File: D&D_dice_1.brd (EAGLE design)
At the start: 27.9 x 31.8 mm, 28 parts, among them SW1 SPST_SWITCH, SW2 SPST_SWITCH, SW3 SPST_SWITCH, SW4 SPST_SWITCH, SW5 SPST_SWITCH, SW6 SPST_SWITCH, U1 ATMEGA168

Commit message: Board, code improvement.
Optimized the code, and improved the board a bit.
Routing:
- net GND: track 50.9 -> 71.2 mm
- net V+: track 91.2 -> 92.3 mm
- net RANDOM_OUT: track 30.1 -> 31.2 mm
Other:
- board text added: "Dice Roller"
- board text removed: "D&D Roller"

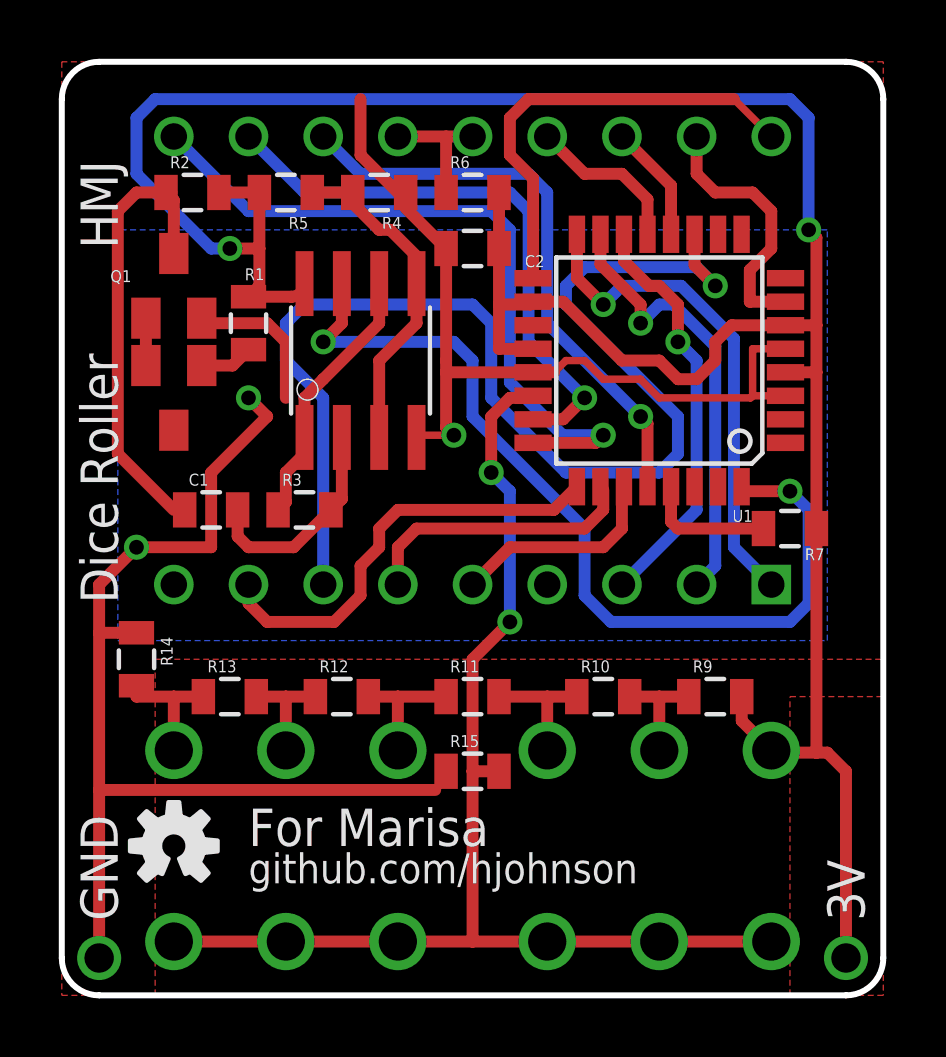
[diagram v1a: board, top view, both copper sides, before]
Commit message: Major commit: TESTED
Boards re-jiggered with bigger 0805 pads, because the small ones were
nightmarish. Code also much improved: It now actually works!
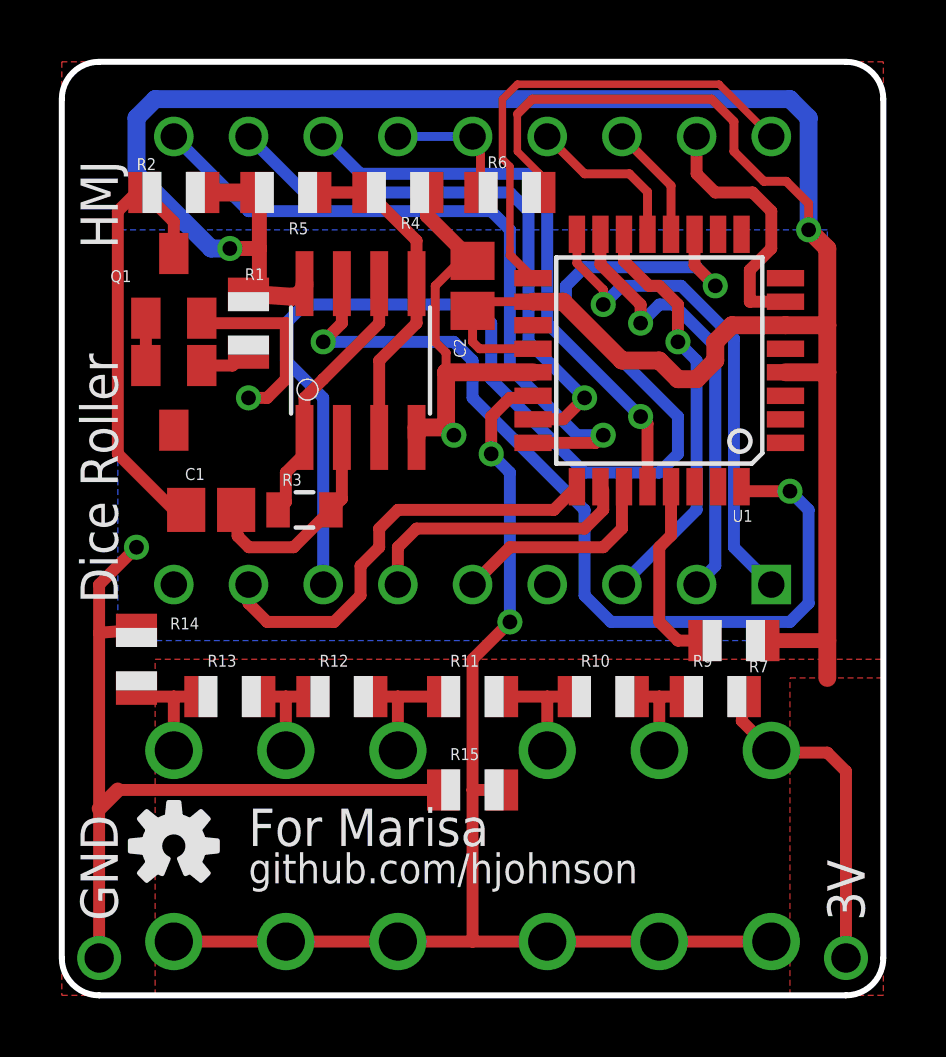
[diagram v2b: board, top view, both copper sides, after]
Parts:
- C1, C2: device SparkFun:0805 -> adafruit:C0805
- R1, R10, R11, R12, R13, R14, R15, R2, R4, R5, R6, R7, R9: device SparkFun:0805 -> adafruit:R0805
- moved R7 4.26 mm to (22.9, 12.1)
- moved C2 1.27 mm to (14.0, 24.1), turned to 270 degrees
- moved R6 1.27 mm to (15.2, 27.3)
- moved R2 0.64 mm to (3.81, 27.3)
- moved R15 0.63 mm to (14.0, 6.99)
- moved R4 0.63 mm to (11.4, 27.3)
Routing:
- net GND: track 71.2 -> 48.9 mm
- net V+: track 92.3 -> 106.9 mm
- net /RES: track 4.43 -> 6.57 mm
- net SCK: track 15.5 -> 16.6 mm
- net N$11: track 5.35 -> 4.56 mm
- net N$2: track 15.7 -> 15.0 mm

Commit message: Slight tweaks to the board to make it easier to solder.
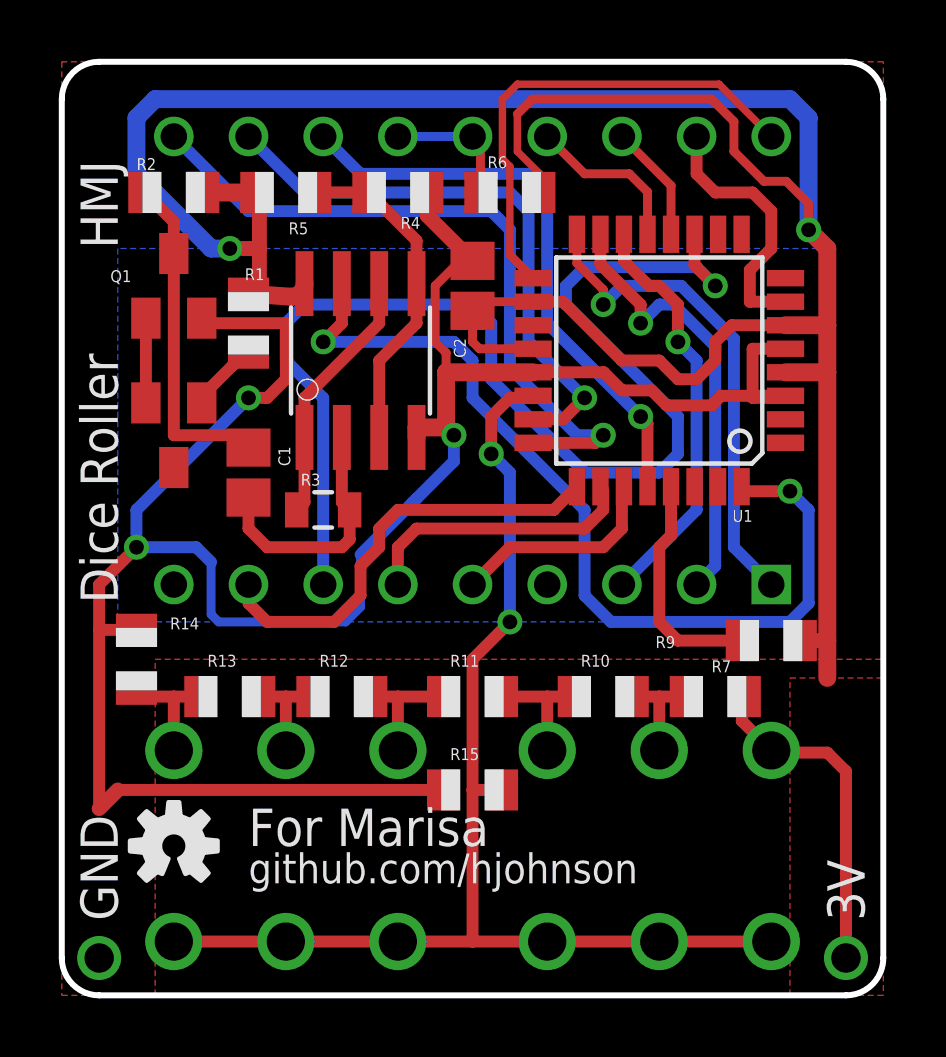
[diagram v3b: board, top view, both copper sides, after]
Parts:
- moved C1 1.80 mm to (6.35, 17.8), turned to 270 degrees
- moved R7 1.27 mm to (24.1, 12.1)
- moved U$1 1.27 mm to (3.81, 19.1)
- moved R3 0.63 mm to (8.89, 16.5)
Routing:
- net GND: track 48.9 -> 80.7 mm
- net N$2: track 15.0 -> 11.7 mm
- net V+: track 106.9 -> 105.7 mm
- net N$1: track 1.61 -> 2.88 mm
- net /RES: track 6.57 -> 7.84 mm
- net N$4: track 7.37 -> 8.45 mm
- net N$3: track 1.75 -> 2.40 mm

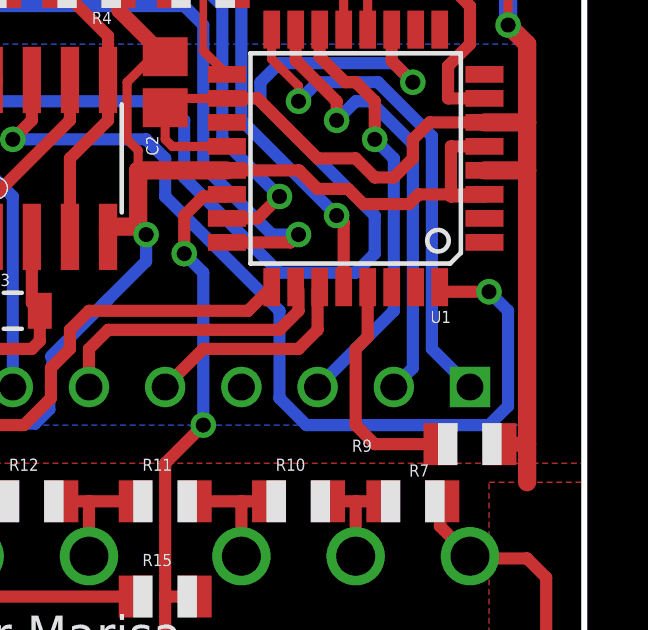
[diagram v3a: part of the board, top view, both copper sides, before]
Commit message: Added test pads for reset, lightly shifted around a few resistors.
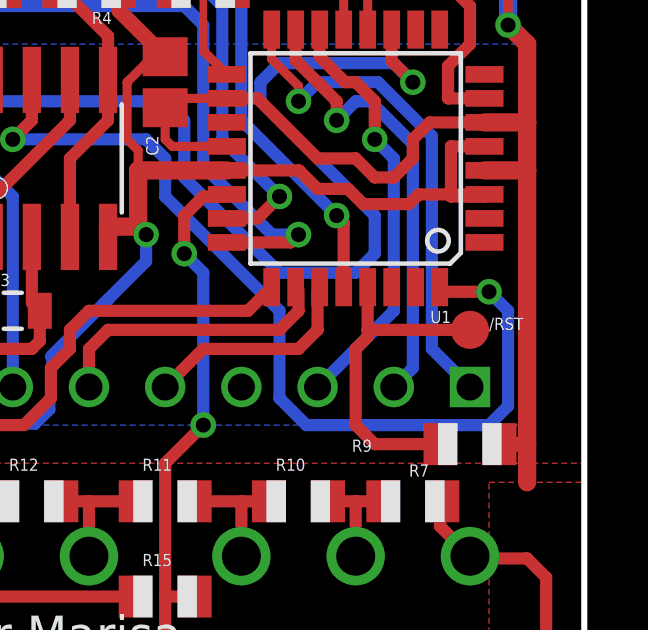
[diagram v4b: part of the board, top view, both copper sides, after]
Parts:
- added TP1: TPB1,27, testpad:B1,27
- IC1: value (none) -> MCP6282-E/SN-ND
- R15: value (none) -> 100K
- R6: value 470 -> 470R
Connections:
- net /RES: now also TP1.TP
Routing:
- net /RES: track 7.84 -> 11.2 mm
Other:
- board text added: "/RST"
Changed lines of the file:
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@@
 <wire x1="8.255" y1="22.86" x2="8.255" y2="20.955" width="0.254" layer="41"/>
 <wire x1="2.54" y1="6.35" x2="12.065" y2="6.35" width="0.254" layer="41"/>
+<text x="24.765" y="15.875" size="0.4064" layer="21">/RST</text>
 </plain>
 <attributes>
@@
 </autorouter>
 <elements>
-<element name="IC1" library="burr-brown" package="SO08" value="" x="10.16" y="21.59" smashed="yes">
+<element name="IC1" library="burr-brown" package="SO08" value="MCP6282-E/SN-ND" x="10.16" y="21.59" smashed="yes">
 <attribute name="OC_NEWARK" value="36K7581" x="38.1" y="-2.54" size="1.778" layer="27" display="off"/>
 <attribute name="MPN" value="OPA2340UA" x="38.1" y="-2.54" size="1.778" layer="27" display="off"/>
 <attribute name="MF" value="TEXAS INSTRUMENTS" x="38.1" y="-2.54" size="1.778" layer="27" display="off"/>
 <attribute name="OC_FARNELL" value="1101541" x="38.1" y="-2.54" size="1.778" layer="27" display="off"/>
-<attribute name="VALUE" x="14.1605" y="19.558" size="1.27" layer="27" ratio="10" rot="R90"/>
 </element>
 <element name="U$1" library="hjohnson_library" package="SOT23" value="" x="3.81" y="19.05" smashed="yes" rot="R180">
@@
 <element name="U1" library="SparkFun" package="TQFP32-08" value="ATMEGA168" x="20.32" y="21.59" rot="R180"/>
 <element name="U$2" library="hjohnson_library" package="HDSP-521E" value="2DIGIT_7SEGMENT" x="13.97" y="21.59" rot="MR0"/>
-<element name="R6" library="adafruit" package="R0805" value="470" x="15.24" y="27.305" smashed="yes">
+<element name="R6" library="adafruit" package="R0805" value="470R" x="15.24" y="27.305" smashed="yes">
 <attribute name="NAME" x="14.478" y="28.1305" size="0.4064" layer="25"/>
 <attribute name="VALUE" x="16.764" y="27.178" size="0.4064" layer="27"/>
@@
 </element>
 <element name="U$3" library="SparkFun" package="OSHW-LOGO-S" value="OSHW-LOGOS" x="3.81" y="5.08"/>
-<element name="R15" library="adafruit" package="R0805" value="" x="13.97" y="6.985" smashed="yes">
+<element name="R15" library="adafruit" package="R0805" value="100K" x="13.97" y="6.985" smashed="yes">
 <attribute name="NAME" x="13.208" y="8.001" size="0.4064" layer="25"/>
 <attribute name="VALUE" x="13.208" y="4.699" size="1.27" layer="27"/>
+</element>
+<element name="TP1" library="testpad" package="B1,27" value="TPB1,27" x="24.13" y="15.875" smashed="yes">
+<attribute name="TP_SIGNAL_NAME" value="" x="23.495" y="13.97" size="1" layer="37"/>
+<attribute name="VALUE" x="23.495" y="15.113" size="0.0254" layer="27"/>
 </element>
 </elements>
@@
 <wire x1="20.955" y1="12.065" x2="20.32" y2="12.7" width="0.4064" layer="1"/>
 <wire x1="20.32" y1="12.7" x2="20.32" y2="15.24" width="0.4064" layer="1"/>
-<wire x1="20.72" y1="17.2974" x2="20.72" y2="15.64" width="0.4064" layer="1"/>
+<wire x1="20.72" y1="17.2974" x2="20.72" y2="15.875" width="0.4064" layer="1"/>
 <wire x1="20.72" y1="15.64" x2="20.32" y2="15.24" width="0.4064" layer="1"/>
+<contactref element="TP1" pad="TP"/>
+<wire x1="24.13" y1="15.875" x2="20.72" y2="15.875" width="0.4064" layer="1"/>
+<wire x1="20.72" y1="15.875" x2="20.72" y2="15.64" width="0.4064" layer="1"/>
 </signal>
 <signal name="RX">

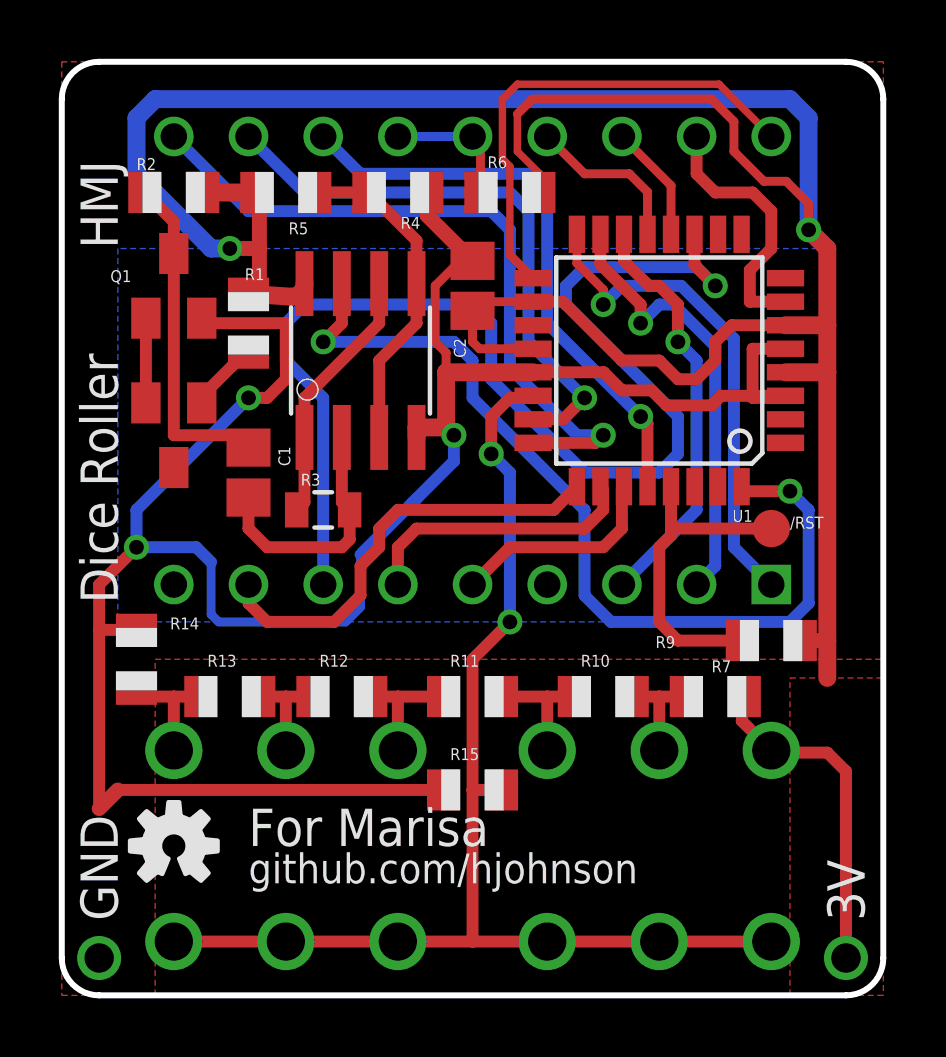
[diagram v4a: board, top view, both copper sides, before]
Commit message: Rotated a capacitor to make schematic look better, and added the schematic pdf.
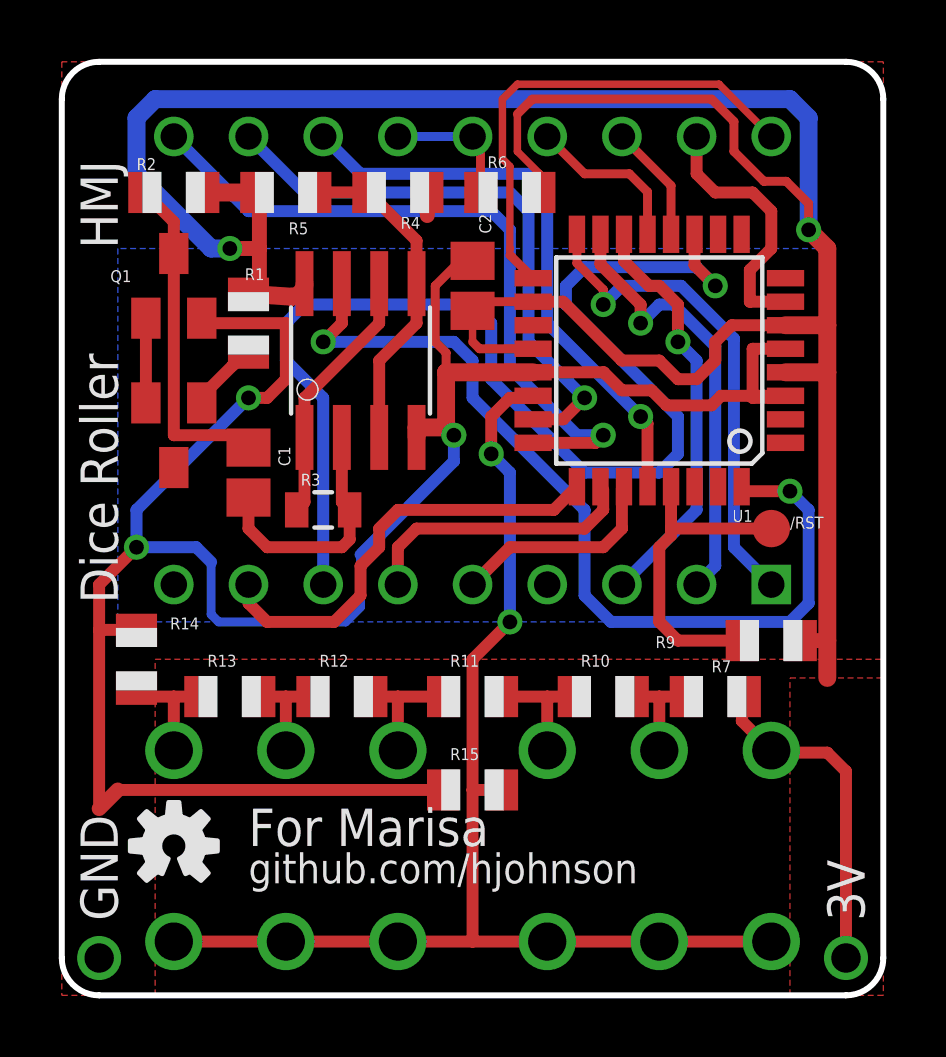
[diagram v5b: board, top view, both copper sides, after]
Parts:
- turned C2 to 90 degrees
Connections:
- net GND: now also C2.2; no longer C2.1
- net V+: now also C2.1; no longer C2.2
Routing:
- net GND: track 80.7 -> 78.1 mm
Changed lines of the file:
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@@
 <attribute name="VALUE" x="7.874" y="18.669" size="0.4064" layer="27" rot="R270"/>
 </element>
-<element name="C2" library="adafruit" package="C0805" value=".1uF" x="13.97" y="24.13" smashed="yes" rot="R270">
-<attribute name="NAME" x="13.335" y="22.352" size="0.4064" layer="25" rot="R270"/>
-<attribute name="VALUE" x="13.843" y="22.606" size="0.4064" layer="27" rot="R270"/>
+<element name="C2" library="adafruit" package="C0805" value=".1uF" x="13.97" y="24.13" smashed="yes" rot="R90">
+<attribute name="NAME" x="14.605" y="25.908" size="0.4064" layer="25" rot="R90"/>
+<attribute name="VALUE" x="14.097" y="25.654" size="0.4064" layer="27" rot="R90"/>
 </element>
 <element name="U1" library="SparkFun" package="TQFP32-08" value="ATMEGA168" x="20.32" y="21.59" rot="R180"/>
@@
 <contactref element="U1" pad="6"/>
 <contactref element="R6" pad="2"/>
-<contactref element="C2" pad="2"/>
 <contactref element="R7" pad="2"/>
 <wire x1="8.255" y1="24.2062" x2="8.255" y2="23.495" width="0.4064" layer="1"/>
@@
 <wire x1="16.0274" y1="21.99" x2="14.205" y2="21.99" width="0.3048" layer="1"/>
 <wire x1="14.205" y1="21.99" x2="13.97" y2="22.225" width="0.3048" layer="1"/>
-<wire x1="13.97" y1="22.225" x2="13.97" y2="23.28" width="0.3048" layer="1"/>
 <wire x1="16.0274" y1="23.59" x2="14.28" y2="23.59" width="0.3048" layer="1"/>
-<wire x1="14.28" y1="23.59" x2="13.97" y2="23.28" width="0.3048" layer="1"/>
 <wire x1="16.24" y1="27.305" x2="16.24" y2="27.448" width="0.3048" layer="1"/>
 <wire x1="15.494" y1="29.972" x2="16.002" y2="30.48" width="0.3048" layer="1"/>
@@
 <wire x1="6.72" y1="27.205" x2="6.62" y2="27.305" width="0.508" layer="1"/>
 <wire x1="5.715" y1="25.4" x2="6.72" y2="25.4" width="0.508" layer="1"/>
+<contactref element="C2" pad="1"/>
+<wire x1="13.97" y1="22.225" x2="13.97" y2="23.28" width="0.254" layer="1"/>
+<wire x1="14.28" y1="23.59" x2="13.97" y2="23.59" width="0.254" layer="1"/>
+<wire x1="13.97" y1="23.59" x2="13.97" y2="23.28" width="0.254" layer="1"/>
 </signal>
 <signal name="A1">
@@
 <contactref element="U1" pad="3"/>
 <contactref element="U1" pad="5"/>
-<contactref element="C2" pad="1"/>
 <wire x1="4.76" y1="23.03" x2="4.91" y2="23.03" width="0.254" layer="1"/>
 <wire x1="4.91" y1="23.03" x2="5.08" y2="22.86" width="0.254" layer="1"/>
@@
 <wire x1="12.7" y1="22.225" x2="12.7" y2="24.13" width="0.3048" layer="1"/>
 <wire x1="12.7" y1="24.13" x2="13.55" y2="24.98" width="0.3048" layer="1"/>
-<wire x1="13.97" y1="24.98" x2="13.55" y2="24.98" width="0.3048" layer="1"/>
 <wire x1="12.43" y1="27.305" x2="12.43" y2="26.52" width="0.508" layer="1"/>
-<wire x1="12.43" y1="26.52" x2="13.97" y2="24.98" width="0.508" layer="1"/>
 <wire x1="12.97" y1="6.985" x2="1.905" y2="6.985" width="0.4064" layer="1"/>
 <wire x1="2.54" y1="12.43" x2="1.27" y2="12.43" width="0.4064" layer="1"/>
@@
 <wire x1="2.54" y1="15.24" x2="2.54" y2="16.51" width="0.4064" layer="16"/>
 <wire x1="2.54" y1="16.51" x2="6.35" y2="20.32" width="0.4064" layer="16"/>
-<wire x1="12.065" y1="16.891" x2="11.938" y2="16.764" width="0.4064" layer="16"/>
-<wire x1="11.938" y1="16.764" x2="10.16" y2="14.986" width="0.4064" layer="16"/>
+<wire x1="13.335" y1="18.161" x2="10.16" y2="14.986" width="0.4064" layer="16"/>
 <wire x1="10.16" y1="14.986" x2="10.16" y2="13.208" width="0.3048" layer="16"/>
 <wire x1="10.16" y1="13.208" x2="9.652" y2="12.7" width="0.3048" layer="16"/>
@@
 <wire x1="4.572" y1="15.24" x2="2.54" y2="15.24" width="0.4064" layer="16"/>
 <wire x1="13.335" y1="19.05" x2="13.335" y2="18.161" width="0.4064" layer="16"/>
-<wire x1="13.335" y1="18.161" x2="12.065" y2="16.891" width="0.4064" layer="16"/>
 <wire x1="13.07" y1="19.315" x2="13.335" y2="19.05" width="0.4064" layer="1"/>
 <wire x1="1.905" y1="6.985" x2="1.27" y2="6.35" width="0.508" layer="1"/>
+<contactref element="C2" pad="2"/>
 </signal>
 </signals>
